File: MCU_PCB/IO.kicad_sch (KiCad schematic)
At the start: 5 parts, among them J1 BackBone, J2 D1, J3 D2

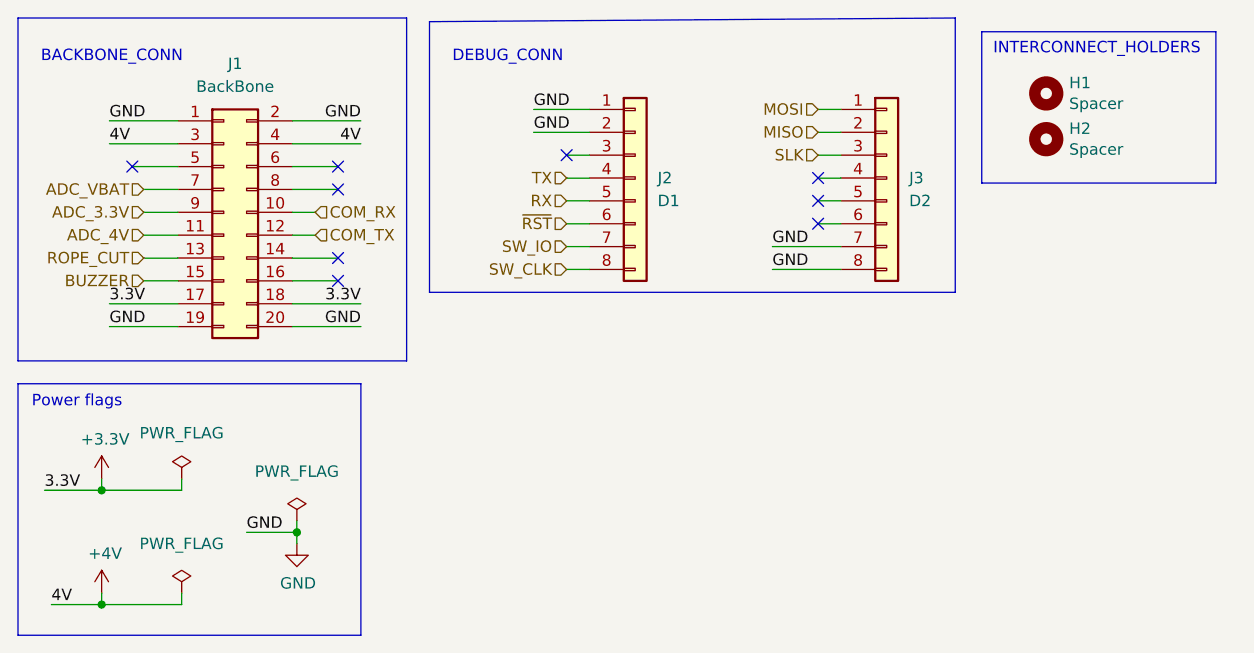
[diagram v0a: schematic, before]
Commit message: 0.1v MCU KiCad
Aesthetics needs to be improved.
Trace width needs to be changed.
More sufficient grounding.
Component placement could be changed.
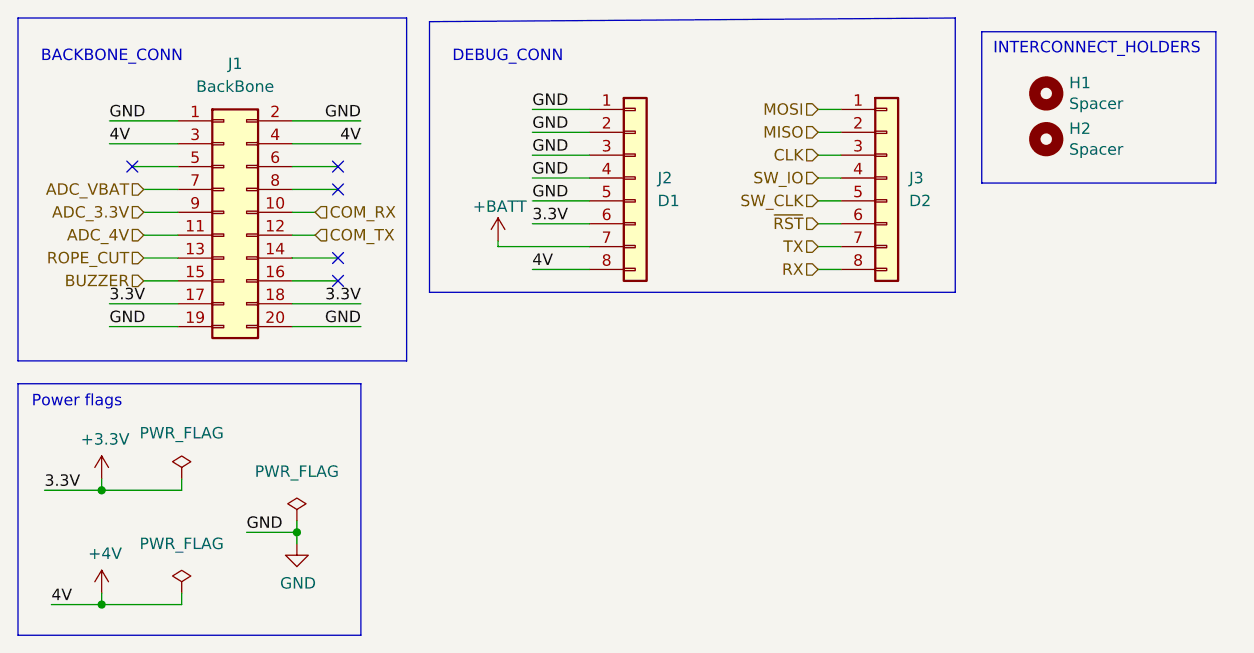
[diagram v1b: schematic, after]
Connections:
- net +3V3: now also J2.6 (Pin_6)
- net +4V: now also J2.8 (Pin_8)
- net GND: now also J2.3 (Pin_3), J2.4 (Pin_4), J2.5 (Pin_5); no longer J3.7 (Pin_7), J3.8 (Pin_8)
- net RX: now also J3.8 (Pin_8); no longer J2.5 (Pin_5)
- net SW_CLK: now also J3.5 (Pin_5); no longer J2.8 (Pin_8)
- net SW_IO: now also J3.4 (Pin_4); no longer J2.7 (Pin_7)
- net TX: now also J3.7 (Pin_7); no longer J2.4 (Pin_4)
- net ~{RST}: now also J3.6 (Pin_6); no longer J2.6 (Pin_6)
- net SLK renamed CLK
- new net +BATT: J2.7 (Pin_7)
- no-connect marks 9 -> 5
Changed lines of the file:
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@@
   (no_connect (at 50.8 41.91))
   (no_connect (at 50.8 44.45))
-  (no_connect (at 104.14 33.02))
-  (no_connect (at 104.14 38.1))
-  (no_connect (at 104.14 35.56))
-  (no_connect (at 76.2 30.48))
   (wire (pts (xy 45.72 39.37) (xy 48.26 39.37))
     (stroke (width 0) (type default) (color 0 0 0 0))
@@
     (stroke (width 0) (type default) (color 0 0 0 0))
   )
-  (wire (pts (xy 78.74 30.48) (xy 76.2 30.48))
-    (stroke (width 0) (type default) (color 0 0 0 0))
-  )
   (wire (pts (xy 45.72 44.45) (xy 50.8 44.45))
     (stroke (width 0) (type default) (color 0 0 0 0))
@@
     (stroke (width 0) (type default) (color 0 0 0 0))
   )
-  (wire (pts (xy 72.5424 27.94) (xy 78.74 27.94))
-    (stroke (width 0) (type default) (color 0 0 0 0))
-  )
-  (wire (pts (xy 76.2 38.1) (xy 78.74 38.1))
+  (wire (pts (xy 104.14 40.64) (xy 106.68 40.64))
     (stroke (width 0) (type default) (color 0 0 0 0))
   )
@@
     (stroke (width 0) (type default) (color 0 0 0 0))
   )
-  (wire (pts (xy 78.74 43.18) (xy 76.2 43.18))
-    (stroke (width 0) (type default) (color 0 0 0 0))
-  )
-  (wire (pts (xy 78.74 33.02) (xy 76.2 33.02))
-    (stroke (width 0) (type default) (color 0 0 0 0))
-  )
-  (wire (pts (xy 99.06 40.64) (xy 106.68 40.64))
+  (wire (pts (xy 72.39 25.4) (xy 78.74 25.4))
     (stroke (width 0) (type default) (color 0 0 0 0))
   )
@@
     (stroke (width 0) (type default) (color 0 0 0 0))
   )
-  (wire (pts (xy 72.5424 25.4) (xy 78.74 25.4))
-    (stroke (width 0) (type default) (color 0 0 0 0))
-  )
   (wire (pts (xy 106.68 27.94) (xy 104.14 27.94))
     (stroke (width 0) (type default) (color 0 0 0 0))
@@
     (stroke (width 0) (type default) (color 0 0 0 0))
   )
+  (wire (pts (xy 72.39 33.02) (xy 78.74 33.02))
+    (stroke (width 0) (type default) (color 0 0 0 0))
+  )
   (wire (pts (xy 45.72 29.21) (xy 53.34 29.21))
     (stroke (width 0) (type default) (color 0 0 0 0))
   )
+  (wire (pts (xy 72.39 38.1) (xy 78.74 38.1))
+    (stroke (width 0) (type default) (color 0 0 0 0))
+  )
   (wire (pts (xy 25.4 46.99) (xy 33.02 46.99))
     (stroke (width 0) (type default) (color 0 0 0 0))
@@
     (stroke (width 0) (type default) (color 0 0 0 0))
   )
+  (wire (pts (xy 68.58 40.64) (xy 68.58 40.005))
+    (stroke (width 0) (type default) (color 0 0 0 0))
+  )
   (wire (pts (xy 29.21 44.45) (xy 33.02 44.45))
     (stroke (width 0) (type default) (color 0 0 0 0))
@@
     (stroke (width 0) (type default) (color 0 0 0 0))
   )
-  (wire (pts (xy 78.74 35.56) (xy 76.2 35.56))
+  (wire (pts (xy 106.68 43.18) (xy 104.14 43.18))
     (stroke (width 0) (type default) (color 0 0 0 0))
   )
@@
     (stroke (width 0) (type default) (color 0 0 0 0))
   )
+  (wire (pts (xy 68.58 40.64) (xy 78.74 40.64))
+    (stroke (width 0) (type default) (color 0 0 0 0))
+  )
   (polyline (pts (xy 15.24 15.24) (xy 58.42 15.24))
     (stroke (width 0) (type default) (color 0 0 0 0))
@@
     (stroke (width 0) (type default) (color 0 0 0 0))
   )
+  (wire (pts (xy 72.39 30.48) (xy 78.74 30.48))
+    (stroke (width 0) (type default) (color 0 0 0 0))
+  )
   (wire (pts (xy 46.228 73.66) (xy 46.228 72.39))
     (stroke (width 0) (type default) (color 0 0 0 0))
   )
+  (wire (pts (xy 72.39 27.94) (xy 78.74 27.94))
+    (stroke (width 0) (type default) (color 0 0 0 0))
+  )
   (wire (pts (xy 29.21 41.91) (xy 33.02 41.91))
     (stroke (width 0) (type default) (color 0 0 0 0))
@@
     (stroke (width 0) (type default) (color 0 0 0 0))
   )
-  (wire (pts (xy 76.2 40.64) (xy 78.74 40.64))
-    (stroke (width 0) (type default) (color 0 0 0 0))
-  )
   (wire (pts (xy 45.72 31.75) (xy 50.8 31.75))
     (stroke (width 0) (type default) (color 0 0 0 0))
   )
+  (wire (pts (xy 72.39 35.56) (xy 78.74 35.56))
+    (stroke (width 0) (type default) (color 0 0 0 0))
+  )
   (polyline (pts (xy 122.3264 16.764) (xy 122.3264 33.5788))
     (stroke (width 0) (type default) (color 0 0 0 0))
@@
     (stroke (width 0) (type default) (color 0 0 0 0))
   )
-  (wire (pts (xy 99.06 43.18) (xy 106.68 43.18))
+  (wire (pts (xy 72.39 43.18) (xy 78.74 43.18))
     (stroke (width 0) (type default) (color 0 0 0 0))
   )
@@
   )
   (text "INTERCONNECT_HOLDERS\n" (at 123.5964 19.4564 0)
+    (effects (font (size 1.27 1.27)) (justify left bottom))
+  )
+  (label "4V" (at 72.39 43.18 0)
     (effects (font (size 1.27 1.27)) (justify left bottom))
   )
@@
     (effects (font (size 1.27 1.27)) (justify right bottom))
   )
-  (label "GND" (at 72.5424 27.94 0)
+  (label "GND" (at 72.39 27.94 0)
+    (effects (font (size 1.27 1.27)) (justify left bottom))
+  )
+  (label "GND" (at 72.39 33.02 0)
     (effects (font (size 1.27 1.27)) (justify left bottom))
   )
@@
     (effects (font (size 1.27 1.27)) (justify left bottom))
   )
+  (label "3.3V" (at 72.39 38.1 0)
+    (effects (font (size 1.27 1.27)) (justify left bottom))
+  )
   (label "3.3V" (at 25.4 46.99 0)
     (effects (font (size 1.27 1.27)) (justify left bottom))
   )
-  (label "GND" (at 99.06 43.18 0)
-    (effects (font (size 1.27 1.27)) (justify left bottom))
-  )
-  (label "GND" (at 99.06 40.64 0)
+  (label "GND" (at 72.39 30.48 0)
     (effects (font (size 1.27 1.27)) (justify left bottom))
   )
@@
     (effects (font (size 1.27 1.27)) (justify right bottom))
   )
-  (label "GND" (at 72.5424 25.4 0)
+  (label "GND" (at 72.39 25.4 0)
+    (effects (font (size 1.27 1.27)) (justify left bottom))
+  )
+  (label "GND" (at 72.39 35.56 0)
     (effects (font (size 1.27 1.27)) (justify left bottom))
   )
@@
     (effects (font (size 1.27 1.27)) (justify right bottom))
   )
-  (hierarchical_label "TX" (shape input) (at 76.2 33.02 180)
-    (effects (font (size 1.27 1.27)) (justify right))
-  )
-  (hierarchical_label "RX" (shape input) (at 76.2 35.56 180)
+  (hierarchical_label "TX" (shape input) (at 104.14 40.64 180)
+    (effects (font (size 1.27 1.27)) (justify right))
+  )
+  (hierarchical_label "RX" (shape input) (at 104.14 43.18 180)
     (effects (font (size 1.27 1.27)) (justify right))
   )
@@
     (effects (font (size 1.27 1.27)) (justify right))
   )
-  (hierarchical_label "SLK" (shape input) (at 104.14 30.48 180)
+  (hierarchical_label "CLK" (shape input) (at 104.14 30.48 180)
     (effects (font (size 1.27 1.27)) (justify right))
   )
@@
     (effects (font (size 1.27 1.27)) (justify left))
   )
-  (hierarchical_label "SW_IO" (shape input) (at 76.2 40.64 180)
-    (effects (font (size 1.27 1.27)) (justify right))
-  )
-  (hierarchical_label "~{RST}" (shape input) (at 76.2 38.1 180)
+  (hierarchical_label "SW_IO" (shape input) (at 104.14 33.02 180)
+    (effects (font (size 1.27 1.27)) (justify right))
+  )
+  (hierarchical_label "~{RST}" (shape input) (at 104.14 38.1 180)
     (effects (font (size 1.27 1.27)) (justify right))
   )
@@
     (effects (font (size 1.27 1.27)) (justify right))
   )
-  (hierarchical_label "SW_CLK" (shape input) (at 76.2 43.18 180)
+  (hierarchical_label "SW_CLK" (shape input) (at 104.14 35.56 180)
     (effects (font (size 1.27 1.27)) (justify right))
   )
@@
     )
   )
+  (symbol (lib_id "power:+BATT") (at 68.58 40.005 0) (unit 1)
+    (in_bom yes) (on_board yes)
+    (property "Reference" "#PWR0166" (id 0) (at 68.58 43.815 0)
+      (effects (font (size 1.27 1.27)) hide)
+    )
+    (property "Value" "+BATT" (id 1) (at 71.755 36.195 0)
+      (effects (font (size 1.27 1.27)) (justify right))
+    )
+    (property "Footprint" "" (id 2) (at 68.58 40.005 0)
+      (effects (font (size 1.27 1.27)) hide)
+    )
+    (property "Datasheet" "" (id 3) (at 68.58 40.005 0)
+      (effects (font (size 1.27 1.27)) hide)
+    )
+    (pin "1")
+  )
 )
